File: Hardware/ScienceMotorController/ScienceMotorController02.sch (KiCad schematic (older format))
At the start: 5 parts, among them U2 TM4C129E_Launchpad

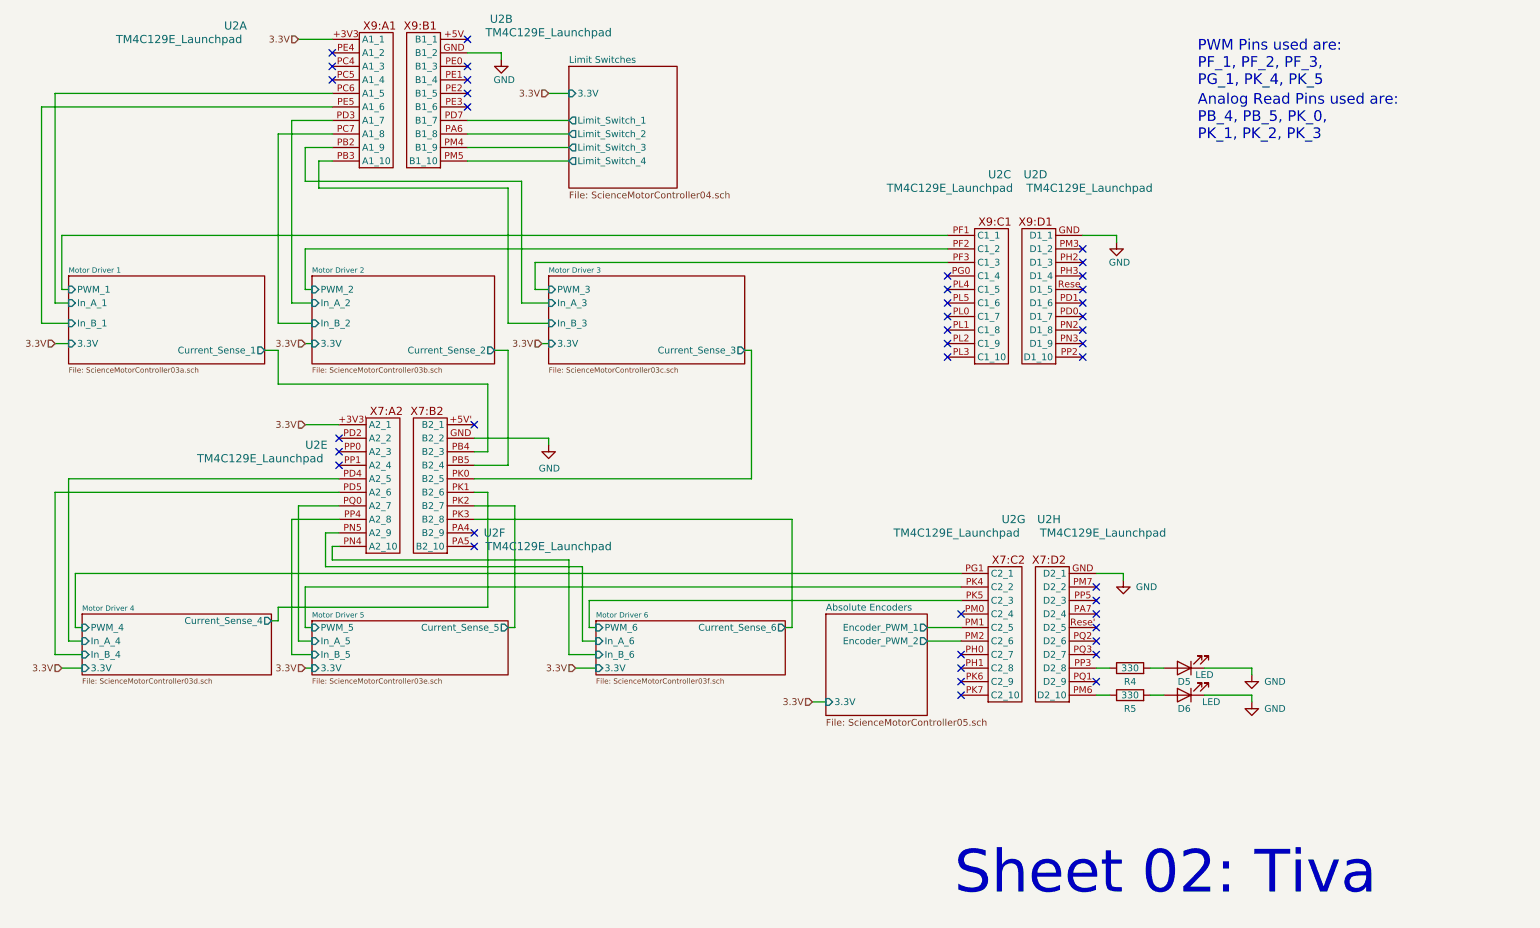
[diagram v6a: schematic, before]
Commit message: running traces
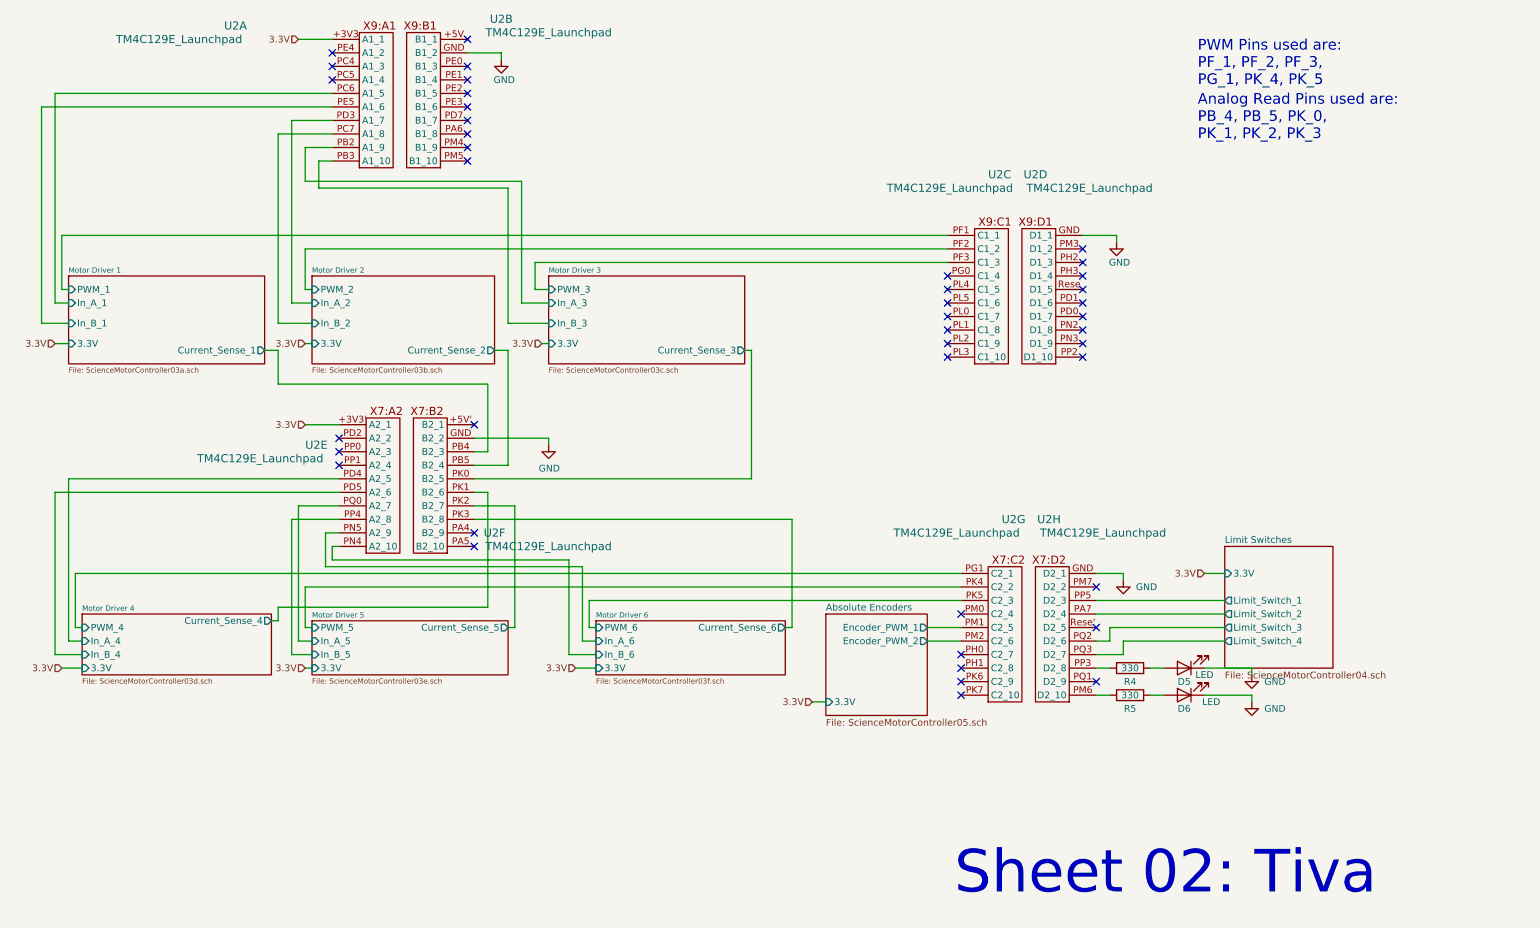
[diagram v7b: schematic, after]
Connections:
- net Limit Switches/Limit_Switch_1: now also U2.PP5 (D2_3); no longer U2.PD7 (B1_7)
- net Limit Switches/Limit_Switch_2: now also U2.PA7 (D2_4); no longer U2.PA6 (B1_8)
- net Limit Switches/Limit_Switch_3: now also U2.PQ2 (D2_6); no longer U2.PM4 (B1_9)
- net Limit Switches/Limit_Switch_4: now also U2.PQ3 (D2_7); no longer U2.PM5 (B1_10)
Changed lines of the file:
@@
 	9400 5500 9750 5500
 NoConn ~ 8600 4700
-NoConn ~ 8600 4800
-NoConn ~ 8600 4900
 NoConn ~ 8600 5000
-NoConn ~ 8600 5100
-NoConn ~ 8600 5200
 NoConn ~ 8600 5400
 NoConn ~ 7600 5500
@@
 	2550 4950 2500 4950
 $Sheet
-S 4700 850  800  900
+S 9550 4400 800  900
 U 5FC42AEE
 F0 "Limit Switches" 50
 F1 "ScienceMotorController04.sch" 50
-F2 "3.3V" I L 4700 1050 50
-F3 "Limit_Switch_1" O L 4700 1250 50
-F4 "Limit_Switch_2" O L 4700 1350 50
-F5 "Limit_Switch_3" O L 4700 1450 50
-F6 "Limit_Switch_4" O L 4700 1550 50
+F2 "3.3V" I L 9550 4600 50
+F3 "Limit_Switch_1" O L 9550 4800 50
+F4 "Limit_Switch_2" O L 9550 4900 50
+F5 "Limit_Switch_3" O L 9550 5000 50
+F6 "Limit_Switch_4" O L 9550 5100 50
 $EndSheet
 Wire Wire Line
@@
 Wire Wire Line
 	6050 2950 6050 3900
-Text HLabel 4550 1050 0    50   Input ~ 0
-3.3V
-Wire Wire Line
-	4550 1050 4700 1050
-Wire Wire Line
-	3950 1250 4700 1250
-Wire Wire Line
-	3950 1350 4700 1350
-Wire Wire Line
-	3950 1450 4700 1450
-Wire Wire Line
-	3950 1550 4700 1550
+Text HLabel 9400 4600 0    50   Input ~ 0
+3.3V
+Wire Wire Line
+	9400 4600 9550 4600
+Wire Wire Line
+	8800 5100 9550 5100
 Text HLabel 900  2900 0    50   Input ~ 0
 3.3V
@@
 Wire Wire Line
 	7350 5100 7600 5100
+Wire Wire Line
+	8600 4800 9550 4800
+Wire Wire Line
+	8600 4900 9550 4900
+Wire Wire Line
+	8800 5100 8800 5200
+Wire Wire Line
+	8800 5200 8600 5200
+Wire Wire Line
+	8700 5000 8700 5100
+Wire Wire Line
+	8700 5100 8600 5100
+Wire Wire Line
+	8700 5000 9550 5000
+NoConn ~ 3950 1250
+NoConn ~ 3950 1350
+NoConn ~ 3950 1450
+NoConn ~ 3950 1550
 $EndSCHEMATC

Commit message: added oki and began rerouting traces
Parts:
- U2: footprint MRDT_Shields:TM4C129E_Launchpad_FULL_THT_TOP -> MRDT_Shields:TM4C129E_Launchpad_FULL_THT_BOTTOM
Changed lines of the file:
@@
 F 0 "U2" H 2150 2650 60  0000 L CNN
 F 1 "TM4C129E_Launchpad" H 1350 2550 60  0000 L CNN
-F 2 "MRDT_Shields:TM4C129E_Launchpad_FULL_THT_TOP" H 3150 1600 60  0001 C CNN
+F 2 "MRDT_Shields:TM4C129E_Launchpad_FULL_THT_BOTTOM" H 3150 1600 60  0001 C CNN
 F 3 "" H 3150 1600 60  0001 C CNN
 	1    3150 1600
@@
 F 0 "U2" H 3300 2700 60  0000 C CNN
 F 1 "TM4C129E_Launchpad" H 2950 2600 60  0000 C CNN
-F 2 "MRDT_Shields:TM4C129E_Launchpad_FULL_THT_TOP" H 3750 1600 60  0001 C CNN
+F 2 "MRDT_Shields:TM4C129E_Launchpad_FULL_THT_BOTTOM" H 3750 1600 60  0001 C CNN
 F 3 "" H 3750 1600 60  0001 C CNN
 	2    3750 1600
@@
 F 0 "U2" H 7800 4450 60  0000 L CNN
 F 1 "TM4C129E_Launchpad" H 7050 4350 60  0000 L CNN
-F 2 "MRDT_Shields:TM4C129E_Launchpad_FULL_THT_TOP" H 7700 3050 60  0001 C CNN
+F 2 "MRDT_Shields:TM4C129E_Launchpad_FULL_THT_BOTTOM" H 7700 3050 60  0001 C CNN
 F 3 "" H 7700 3050 60  0001 C CNN
 	3    7700 3050
@@
 F 0 "U2" H 8450 4450 60  0000 C CNN
 F 1 "TM4C129E_Launchpad" H 8050 4350 60  0000 C CNN
-F 2 "MRDT_Shields:TM4C129E_Launchpad_FULL_THT_TOP" H 8300 3050 60  0001 C CNN
+F 2 "MRDT_Shields:TM4C129E_Launchpad_FULL_THT_BOTTOM" H 8300 3050 60  0001 C CNN
 F 3 "" H 8300 3050 60  0001 C CNN
 	4    8300 3050
@@
 F 0 "U2" H 2750 5250 60  0000 L CNN
 F 1 "TM4C129E_Launchpad" H 1950 5150 60  0000 L CNN
-F 2 "MRDT_Shields:TM4C129E_Launchpad_FULL_THT_TOP" H 3200 4450 60  0001 C CNN
+F 2 "MRDT_Shields:TM4C129E_Launchpad_FULL_THT_BOTTOM" H 3200 4450 60  0001 C CNN
 F 3 "" H 3200 4450 60  0001 C CNN
 	5    3200 4450
@@
 F 0 "U2" H 3450 4600 60  0000 C CNN
 F 1 "TM4C129E_Launchpad" H 3050 4500 60  0000 C CNN
-F 2 "MRDT_Shields:TM4C129E_Launchpad_FULL_THT_TOP" H 3800 4450 60  0001 C CNN
+F 2 "MRDT_Shields:TM4C129E_Launchpad_FULL_THT_BOTTOM" H 3800 4450 60  0001 C CNN
 F 3 "" H 3800 4450 60  0001 C CNN
 	6    3800 4450
@@
 F 0 "U2" H 7900 6900 60  0000 L CNN
 F 1 "TM4C129E_Launchpad" H 7100 6800 60  0000 L CNN
-F 2 "MRDT_Shields:TM4C129E_Launchpad_FULL_THT_TOP" H 7800 5550 60  0001 C CNN
+F 2 "MRDT_Shields:TM4C129E_Launchpad_FULL_THT_BOTTOM" H 7800 5550 60  0001 C CNN
 F 3 "" H 7800 5550 60  0001 C CNN
 	7    7800 5550
@@
 F 0 "U2" H 8550 6900 60  0000 C CNN
 F 1 "TM4C129E_Launchpad" H 8150 6800 60  0000 C CNN
-F 2 "MRDT_Shields:TM4C129E_Launchpad_FULL_THT_TOP" H 8400 5550 60  0001 C CNN
+F 2 "MRDT_Shields:TM4C129E_Launchpad_FULL_THT_BOTTOM" H 8400 5550 60  0001 C CNN
 F 3 "" H 8400 5550 60  0001 C CNN
 	8    8400 5550
